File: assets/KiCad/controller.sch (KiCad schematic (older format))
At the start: 1 part

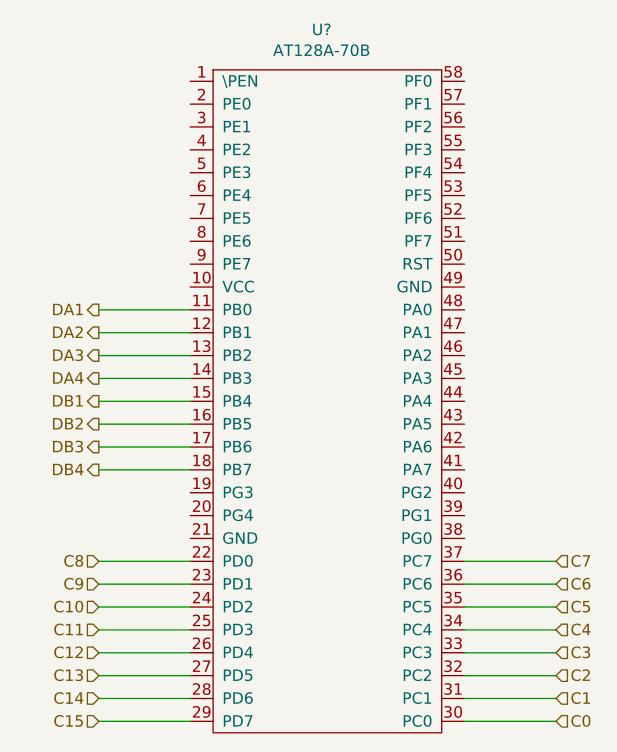
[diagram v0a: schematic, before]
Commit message: schematic update
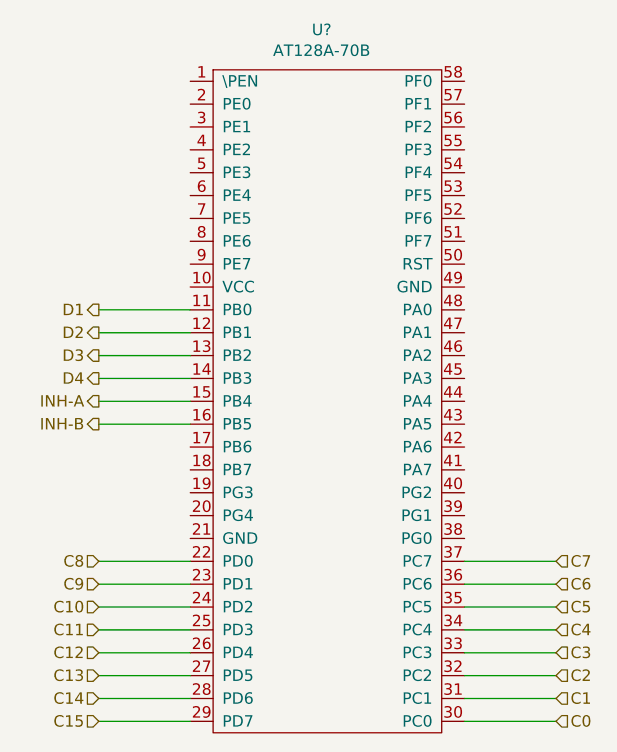
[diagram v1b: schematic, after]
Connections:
- net DA1 renamed D1
- net DA2 renamed D2
- net DA3 renamed D3
- net DA4 renamed D4
- net DB1 renamed INH-A
- net DB2 renamed INH-B
- net DB3: no longer names the net of U?.17 (PB6)
- net DB4: no longer names the net of U?.18 (PB7)
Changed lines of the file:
@@
 	5000 3850 5400 3850
-Wire Wire Line
-	5000 3950 5400 3950
-Wire Wire Line
-	5000 4050 5400 4050
-Wire Wire Line
-	5000 4150 5400 4150
-Wire Wire Line
-	5000 4250 5400 4250
 Wire Wire Line
 	6600 5350 7000 5350
@@
 	5000 5350 5400 5350
 Text HLabel 5000 3550 0    50   Output ~ 0
-DA1
+D1
 Text HLabel 5000 3650 0    50   Output ~ 0
-DA2
+D2
 Text HLabel 5000 3750 0    50   Output ~ 0
-DA3
+D3
 Text HLabel 5000 3850 0    50   Output ~ 0
-DA4
-Text HLabel 5000 3950 0    50   Output ~ 0
-DB1
-Text HLabel 5000 4050 0    50   Output ~ 0
-DB2
-Text HLabel 5000 4150 0    50   Output ~ 0
-DB3
-Text HLabel 5000 4250 0    50   Output ~ 0
-DB4
+D4
 Text HLabel 7000 5350 2    50   Input ~ 0
 C0
@@
 Text HLabel 5000 5350 0    50   Input ~ 0
 C15
+Wire Wire Line
+	5400 3950 5000 3950
+Wire Wire Line
+	5000 4050 5400 4050
+Text HLabel 5000 3950 0    50   Output ~ 0
+INH-A
+Text HLabel 5000 4050 0    50   Output ~ 0
+INH-B
 $EndSCHEMATC

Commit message: update schematics
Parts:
- gave numbers to parts that had none: 1
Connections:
- net VCC: now reaches U3.10 (VCC)
- net GND: now reaches U3.21 (GND)
- net GND: now also U3.49 (GND)
- no-connect marks 0 -> 33
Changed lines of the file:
@@
 $Descr A4 11693 8268
 encoding utf-8
-Sheet 5 8
+Sheet 8 8
 Title ""
 Date ""
@@
 $EndDescr
 $Comp
-L MyICs:AT128A-70B U?
+L MyICs:AT128A-70B U3
 U 1 1 5F5DCF09
 P 6000 3900
-F 0 "U?" H 5975 5475 50  0000 C CNN
+F 0 "U3" H 5975 5475 50  0000 C CNN
 F 1 "AT128A-70B" H 5975 5384 50  0000 C CNN
 F 2 "" H 5950 5050 50  0001 C CNN
@@
 Text HLabel 5000 4050 0    50   Output ~ 0
 INH-B
+$Comp
+L power:VCC #PWR?
+U 1 1 5F72768F
+P 5250 3450
+F 0 "#PWR?" H 5250 3300 50  0001 C CNN
+F 1 "VCC" H 5267 3623 50  0000 C CNN
+F 2 "" H 5250 3450 50  0001 C CNN
+F 3 "" H 5250 3450 50  0001 C CNN
+	1    5250 3450
+	1    0    0    -1
+$EndComp
+$Comp
+L power:GND #PWR?
+U 1 1 5F72B496
+P 6750 3450
+F 0 "#PWR?" H 6750 3200 50  0001 C CNN
+F 1 "GND" H 6755 3277 50  0000 C CNN
+F 2 "" H 6750 3450 50  0001 C CNN
+F 3 "" H 6750 3450 50  0001 C CNN
+	1    6750 3450
+	1    0    0    -1
+$EndComp
+$Comp
+L power:GND #PWR?
+U 1 1 5F72BC5E
+P 5250 4350
+F 0 "#PWR?" H 5250 4100 50  0001 C CNN
+F 1 "GND" H 5255 4177 50  0000 C CNN
+F 2 "" H 5250 4350 50  0001 C CNN
+F 3 "" H 5250 4350 50  0001 C CNN
+	1    5250 4350
+	1    0    0    -1
+$EndComp
+Wire Wire Line
+	5400 4550 5350 4550
+Wire Wire Line
+	5350 4550 5350 4350
+Wire Wire Line
+	5350 4350 5250 4350
+NoConn ~ 5400 2550
+NoConn ~ 5400 2650
+NoConn ~ 5400 2750
+NoConn ~ 5400 2850
+NoConn ~ 5400 2950
+NoConn ~ 5400 3050
+NoConn ~ 5400 3150
+NoConn ~ 5400 3250
+NoConn ~ 5400 3350
+NoConn ~ 5400 4150
+NoConn ~ 5400 4250
+NoConn ~ 5400 4350
+NoConn ~ 5400 4450
+NoConn ~ 6600 4550
+NoConn ~ 6600 4450
+NoConn ~ 6600 4350
+NoConn ~ 6600 4250
+NoConn ~ 6600 4150
+NoConn ~ 6600 4050
+NoConn ~ 6600 3950
+NoConn ~ 6600 3850
+NoConn ~ 6600 3750
+NoConn ~ 6600 3650
+NoConn ~ 6600 3550
+NoConn ~ 6600 2550
+NoConn ~ 6600 2650
+NoConn ~ 6600 2750
+NoConn ~ 6600 2850
+NoConn ~ 6600 2950
+NoConn ~ 6600 3050
+NoConn ~ 6600 3150
+NoConn ~ 6600 3250
+NoConn ~ 6600 3350
+Wire Wire Line
+	5250 3450 5400 3450
+Wire Wire Line
+	6600 3450 6750 3450
 $EndSCHEMATC
